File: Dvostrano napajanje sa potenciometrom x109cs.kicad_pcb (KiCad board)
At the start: 2 copper layers, 203.6 x 133.9 mm, 74 parts, among them J2 1, J3 1, J4 Conn_01x04, J5 FLAT za displej, J6 703W-00/08, Q1 2SA1837, Q2 2SA4793, T1 VPP28–090, U1 X9C103S, U2 LM337_TO220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

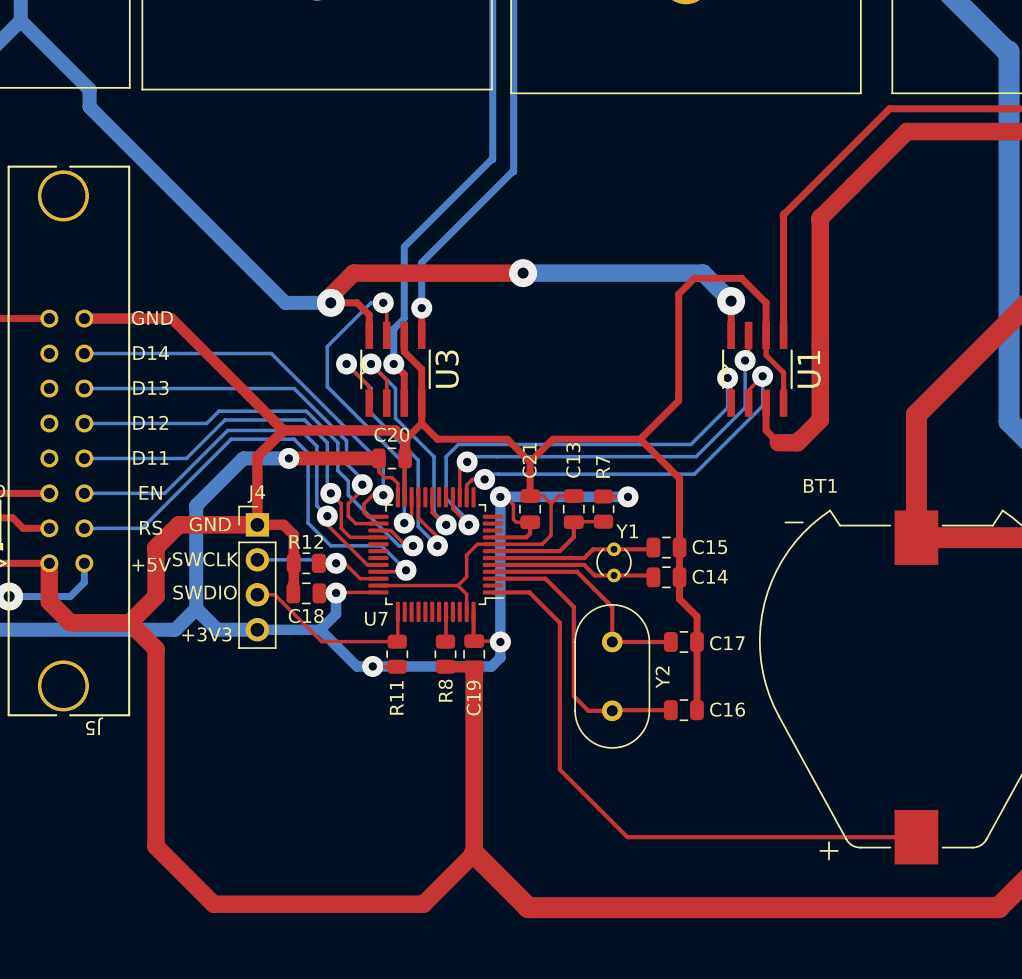
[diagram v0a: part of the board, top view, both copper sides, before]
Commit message: Postavljen je Switch na šematiku za mikrokontroler, takođe je povezan na PCB-u.
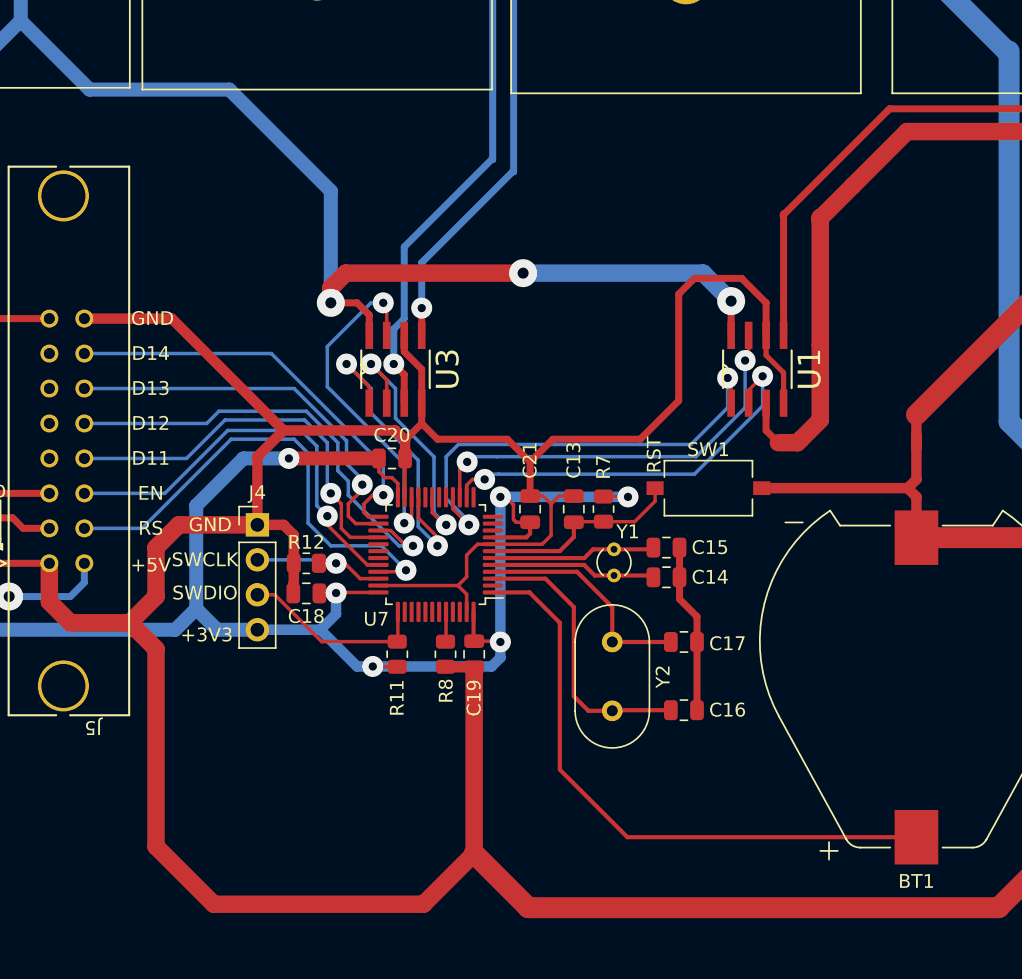
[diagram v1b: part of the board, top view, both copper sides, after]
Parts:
- added SW1: SW_Push, Button_Switch_SMD:SW_Tactile_SPST_NO_Straight_CK_PTS636Sx25SMTRLFS, F.Cu at (269.6, 300.6)
- C6: value 100nF/16V -> 100uF/25V
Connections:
- net /Dual supply/V_H+ renamed Net-(R2-Pad2)
- net /Dual supply/V_H- renamed Net-(R1-Pad2)
- U1 pad 4: GND -> unconnected-(U1-Pad4)
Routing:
- net /MCU/RST: track 9.55 -> 14.9 mm
- net /+5V: track 187.5 -> 191.9 mm
- net GND: track 801.9 -> 804.9 mm
